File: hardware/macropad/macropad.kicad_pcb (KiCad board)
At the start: 2 copper layers, 157.2 x 88.1 mm, 85 parts, among them J1 SWD, J10 Conn_01x02, J2 USB_C_Receptacle_USB2.0_16P, J3 Conn_01x02, J4 display(4x1), J5 Conn_01x04_Pin, J6 Enc2, J7 Enc1, J8 Conn_01x02, J9 USB_A, Q1 Q_PMOS, Q2 FS8205A, SW1 SW_Push, SW10 SW_SPDT, SW11 SW_SPDT, SW2 SW_Push, SW3 SW_Push, SW4 SW_Push, SW5 SW_Push, SW6 SW_Push, SW7 SW_Push, SW8 SW_Push, SW9 SW_Push, U1 LP2992IM5-3.3/NOPB, U2 STM32F103C8Tx, U3 NRF24L01_Breakout, U4 STM32F103C8Tx, U5 NRF24L01_Breakout, U6 TP4056-42-ESOP8, U7 DW01A, U8 RT8010AGQW, U9 LP2992IM5-3.3/NOPB, Y1 8Mhz C_L=12pF, Y2 8Mhz

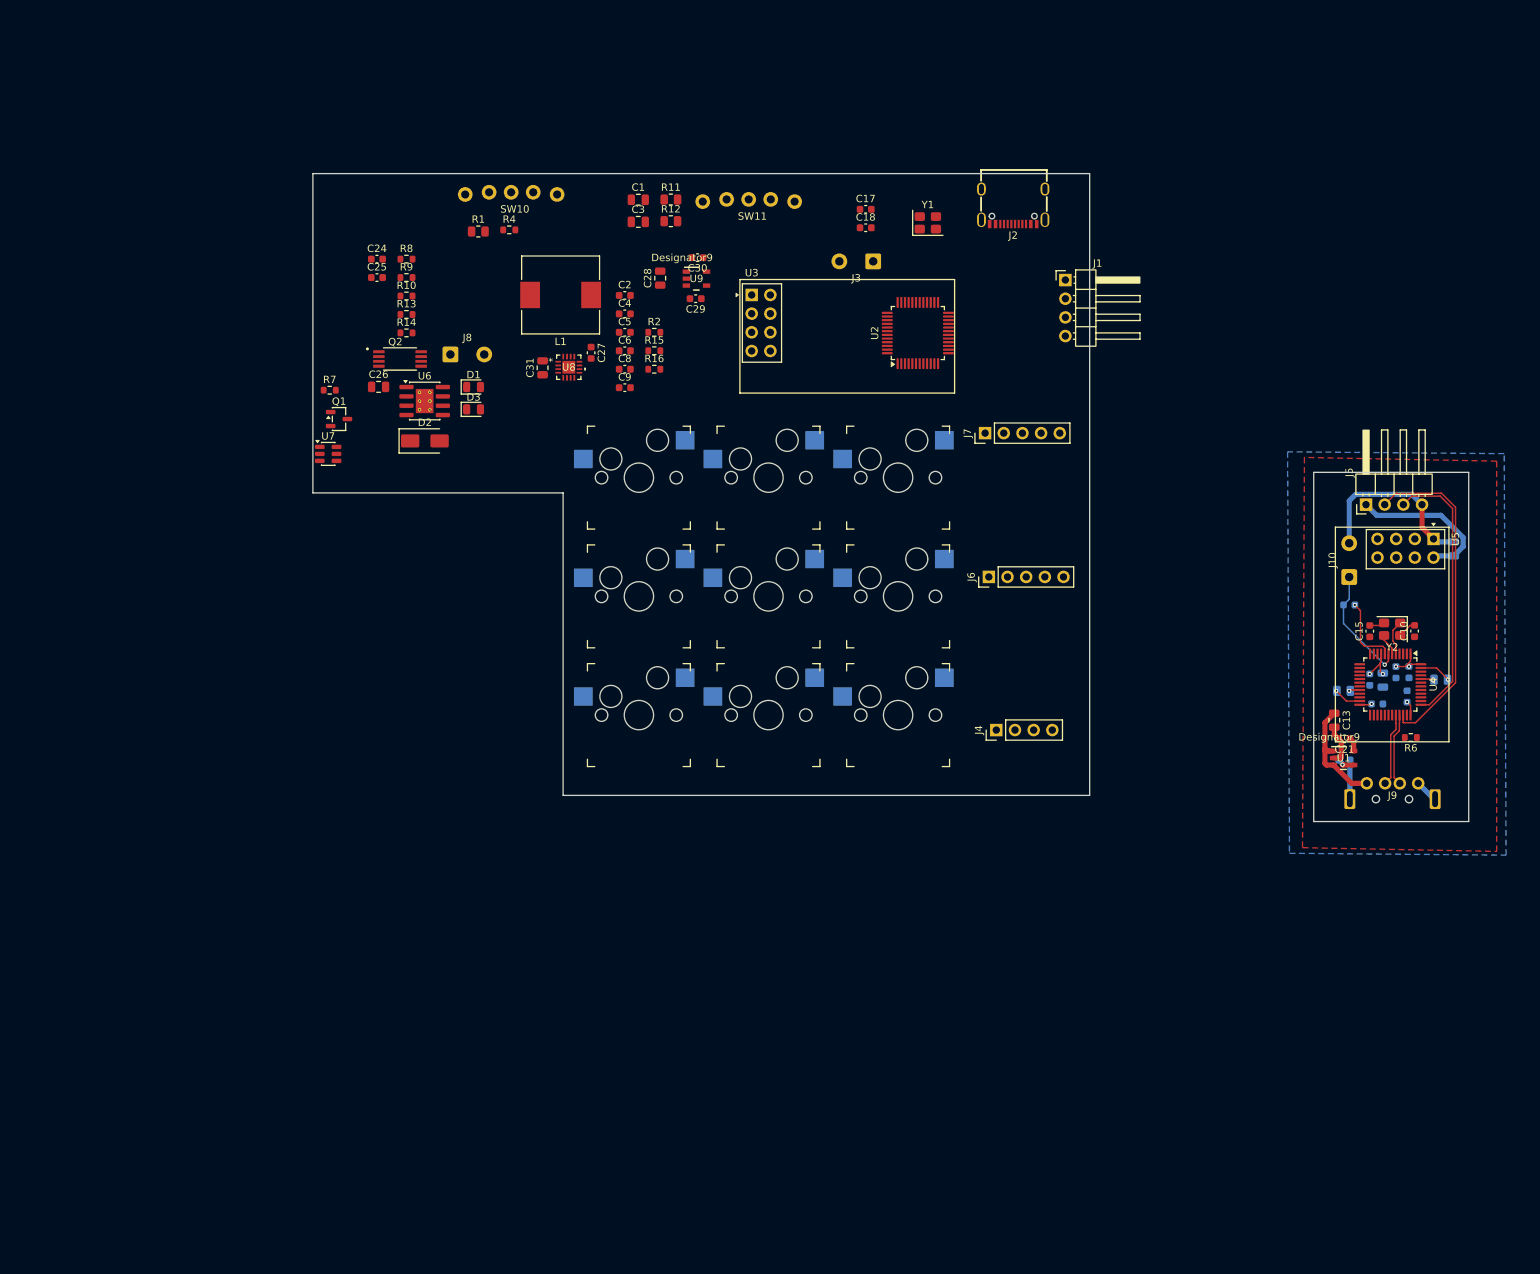
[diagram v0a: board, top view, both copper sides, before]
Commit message: pcb macropad done
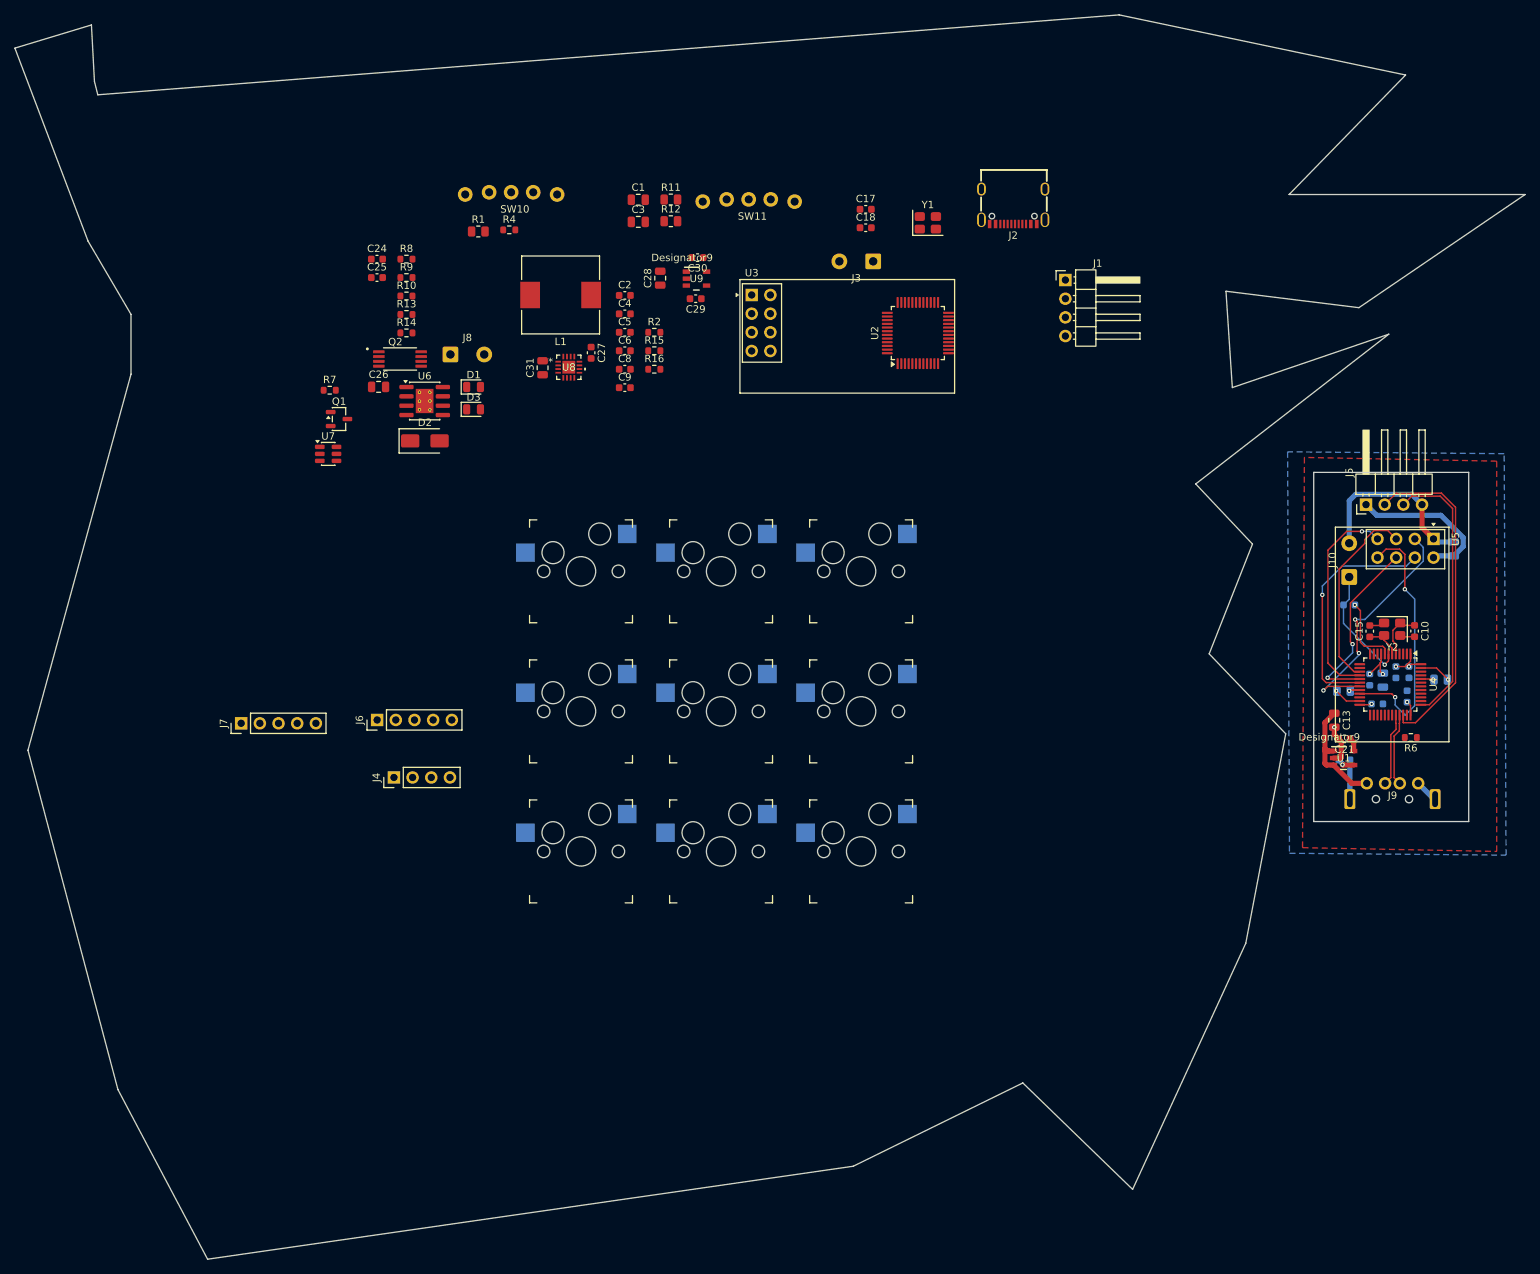
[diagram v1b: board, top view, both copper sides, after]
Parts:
- moved J7 108.6 mm to (42.8, 106.3)
- moved J6 85.5 mm to (61.3, 105.8)
- moved J4 82.2 mm to (63.6, 113.6)
- moved SW3 20.1 mm to (89.1, 123.7)
- moved SW6 19.6 mm to (108.1, 123.7)
- moved SW9 19.2 mm to (127.2, 123.7)
- moved SW2 17.5 mm to (89.1, 104.6)
- moved SW5 16.9 mm to (108.1, 104.6)
- moved SW8 16.4 mm to (127.2, 104.6)
- moved SW1 15.0 mm to (89.1, 85.6)
- moved SW4 14.3 mm to (108.1, 85.6)
- moved SW7 13.7 mm to (127.2, 85.6)
- turned C10 to -90 degrees
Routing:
- net /dongle/PB10_DGL: track 0.00 -> 35.5 mm, vias 0 -> 2
- net /dongle/PB1_DGL: track 0.00 -> 33.1 mm, vias 0 -> 3
- net /dongle/PB0_DGL: track 0.00 -> 32.1 mm, vias 0 -> 1
- net /dongle/PA6_DGL: track 0.00 -> 28.6 mm, vias 0 -> 1
- net /dongle/PA5_DGL: track 0.00 -> 26.3 mm
- net /dongle/PA7_DGL: track 0.00 -> 24.9 mm, vias 0 -> 2
- net /dongle/HSE_IN_DGL: track 4.79 -> 6.87 mm
- net /dongle/HSE_OUT_DGL: track 2.96 -> 4.99 mm
- net GND_DGL: track 61.8 -> 61.3 mm, vias 3 -> 4
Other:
- board size 157.2 x 88.1 mm -> 205.4 x 169.3 mm

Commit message: pcb done
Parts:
- removed J6: Enc2, Connector_PinHeader_2.54mm:PinHeader_1x05_P2.54mm_Vertical
- removed J7: Enc1, Connector_PinHeader_2.54mm:PinHeader_1x05_P2.54mm_Vertical
- added R17: 10k, Resistor_SMD:R_0805_2012Metric, B.Cu at (69.3, 86.2)
- added R18: 10k, Resistor_SMD:R_0805_2012Metric, B.Cu at (69.4, 96.6)
- added R19: 10k, Resistor_SMD:R_0805_2012Metric, B.Cu at (69.4, 99.6)
- added R20: 10k, Resistor_SMD:R_0805_2012Metric, B.Cu at (69.4, 102.5)
- added SW12: RotaryEncoder_Switch, Rotary_Encoder:RotaryEncoder_Alps_EC12E-Switch_Vertical_H20mm, F.Cu at (58.8, 81.2)
- added SW13: RotaryEncoder_Switch, Rotary_Encoder:RotaryEncoder_Alps_EC12E-Switch_Vertical_H20mm, F.Cu at (58.8, 97.0)
- R13: value 1k -> 10k; footprint Resistor_SMD:R_0603_1608Metric -> Resistor_SMD:R_0805_2012Metric; moved to B.Cu
- R14: value 100 -> 10k; footprint Resistor_SMD:R_0603_1608Metric -> Resistor_SMD:R_0805_2012Metric; moved to B.Cu
- U2: moved to B.Cu
- moved U2 67.3 mm to (103.7, 112.8)
- moved R13 30.7 mm to (69.6, 81.1), turned to 180 degrees
- moved R14 30.7 mm to (69.6, 83.6), turned to 180 degrees
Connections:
- R13 pad 1: Net-(U7-CS) -> /ENC1SW_PA2
- R13 pad 2: /Power/out- -> +3.3V
- R14 pad 1: Net-(U7-VCC) -> /ENC1DT_PA0
- R14 pad 2: /Power/B+ -> +3.3V
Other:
- outline, holes or cut-outs redrawn

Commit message: Updated Layout
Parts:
- C1, C17, C18, C2, C3, C4, C5, C6, R11, R12, R2, Y1: moved to B.Cu
- moved J1 108.5 mm to (47.5, 31.0)
- moved Q1 91.1 mm to (146.6, 54.5)
- moved J2 90.1 mm to (64.2, 69.5), turned to -90 degrees
- moved C31 90.1 mm to (172.3, 40.9)
- moved C25 90.1 mm to (149.7, 28.6)
- moved C26 90.1 mm to (150.0, 43.5)
- moved J8 90.1 mm to (159.7, 39.1)
- moved SW10 90.1 mm to (168.0, 17.3)
- moved C27 90.1 mm to (178.9, 38.8)
- moved L1 90.1 mm to (174.7, 31.0)
- moved Q2 90.1 mm to (152.9, 39.7)
- moved R10 90.1 mm to (153.8, 31.1)
- moved R9 90.1 mm to (153.8, 28.6)
- moved U8 88.9 mm to (175.8, 48.6)
- moved C24 86.4 mm to (146.0, 60.0), turned to -90 degrees
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
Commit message: Updated Layout
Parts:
- C3: moved to F.Cu
- moved SW10 61.2 mm to (118.5, 53.2)
- moved C29 34.6 mm to (133.5, 29.5), turned to 0 degrees
- moved C25 33.8 mm to (158.2, 61.3), turned to 90 degrees
- moved R9 33.0 mm to (151.4, 61.5), turned to 180 degrees
- moved C28 31.6 mm to (126.2, 28.4), turned to -90 degrees
- moved R10 31.2 mm to (160.2, 61.7), turned to -90 degrees
- moved C3 29.8 mm to (81.2, 62.5), turned to -90 degrees
- moved SW11 28.7 mm to (139.5, 43.0)
- moved C27 27.9 mm to (151.0, 39.3)
- moved U9 27.3 mm to (129.6, 28.5)
- moved U7 27.2 mm to (155.1, 61.5)
- moved Q2 25.8 mm to (153.4, 65.5), turned to 180 degrees
- moved C30 24.3 mm to (133.5, 27.5), turned to 0 degrees
- moved C26 23.7 mm to (158.8, 65.5), turned to -90 degrees
- moved U8 23.3 mm to (154.2, 39.8), turned to -90 degrees
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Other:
- outline, holes or cut-outs redrawn

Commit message: updated schematic and drc
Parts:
- added R21: 1M, Resistor_SMD:R_0603_1608Metric, F.Cu at (77.4, 32.5)
- added R22: 1M, Resistor_SMD:R_0603_1608Metric, F.Cu at (83.8, 29.6)
- added R23: 10k, Resistor_SMD:R_0805_2012Metric, F.Cu at (77.6, 29.8)
- added R24: 5.1k, Resistor_SMD:R_0603_1608Metric, F.Cu at (77.4, 35.0)
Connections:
- SW13 pad A: /ENC2DT_PA3 -> /ENC2DT_PA8
- SW13 pad B: /ENC2CLK_PA4 -> /ENC2CLK_PA9
- SW13 pad S1: /ENC2SW_PA8 -> /ENC2SW_PA10
- U2 pad 13: /ENC2DT_PA3 -> /VBUS_DET
- U2 pad 14: /ENC2CLK_PA4 -> unconnected-(U2-PA4-Pad14)
- U2 pad 29: /ENC2SW_PA8 -> /ENC2DT_PA8
- U2 pad 30: unconnected-(U2-PA9-Pad30) -> /ENC2CLK_PA9
- U2 pad 31: unconnected-(U2-PA10-Pad31) -> /ENC2SW_PA10

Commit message: Macropad layout kinda done
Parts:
- C1, C17, C18, C2, C4, C5, C6, R11, R12, R13, R14, R17, R18, R19, R2, R20, U2, Y1: moved to F.Cu
- J1: footprint Connector_PinHeader_2.54mm:PinHeader_1x04_P2.54mm_Horizontal -> Connector_PinHeader_2.54mm:PinHeader_1x04_P2.54mm_Vertical
- U3, U5: footprint RF_Module:nRF24L01_Breakout -> nrf24l01:nRF24L01_Breakout
- moved R22 120.7 mm to (201.2, 57.3)
- moved SW11 103.9 mm to (242.2, 26.9)
- moved R10 95.7 mm to (67.0, 83.0), turned to 0 degrees
- moved C25 94.7 mm to (66.6, 85.0), turned to 180 degrees
- moved U7 92.3 mm to (66.8, 88.2), turned to 90 degrees
- moved C26 90.1 mm to (70.7, 84.5), turned to 0 degrees
- moved R9 89.9 mm to (66.8, 91.9), turned to -90 degrees
- moved C24 89.2 mm to (55.1, 88.2), turned to 180 degrees
- moved R1 86.7 mm to (55.1, 86.2), turned to 180 degrees
- moved Q2 86.2 mm to (70.8, 89.9), turned to -90 degrees
- moved J8 84.4 mm to (74.6, 78.5)
- moved D1 83.9 mm to (53.9, 82.8), turned to -90 degrees
- moved D2 82.9 mm to (59.1, 85.2), turned to -90 degrees
- moved D3 82.6 mm to (53.9, 78.6), turned to -90 degrees
- moved R4 78.2 mm to (55.9, 81.1), turned to -90 degrees
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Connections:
- R18 pad 1: /ENC2SW_PA8 -> /ENC2SW_PA10
- R19 pad 1: /ENC2DT_PA3 -> /ENC2CLK_PA9
- R20 pad 1: /ENC2CLK_PA4 -> /ENC2DT_PA8
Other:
- board size 205.4 x 169.3 mm -> 158.4 x 77 mm
- board text added: "BATTERY-18650"
- board text added: "BATTERY-21700"

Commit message: added drc
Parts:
- moved J3 2.71 mm to (97.8, 48.9)
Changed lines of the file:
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@@
 	(footprint "Connector_Wire:SolderWire-0.5sqmm_1x02_P4.6mm_D0.9mm_OD2.1mm"
 		(layer "F.Cu")
-		(at 98.55 51.5)
+		(at 97.79 48.895)
 		(descr "Soldered wire connection, for 2 times 0.5 mm² wires, basic insulation, conductor diameter 0.9mm, outer diameter 2.1mm, size source Multi-Contact FLEXI-E 0.50 (https://www.staubli.com/content/dam/ecs/catalogs-brochures/TM/CAB-Main-11014119-en.pdf#page=9), bend radius 3 times outer diameter, generated with kicad-footprint-generator")
 		(tags "connector wire 0.5sqmm")
